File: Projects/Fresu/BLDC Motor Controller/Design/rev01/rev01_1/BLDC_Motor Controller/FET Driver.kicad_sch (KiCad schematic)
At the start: 0 parts

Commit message: UPDATE 7
COMPLETED MOSFET SCHEMATIC
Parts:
- added C18, C19, C20, C21, C25: 2u2, symbol Device:C
- added C22, C29: 10n, symbol Device:C
- added C23: 120p, symbol Device:C
- added C24: 22n, symbol Device:C
- added C26, C27, C28, C31, C34, C37: 100n, symbol Device:C
- added C30, C32, C33, C35, C36, C38, C39, C40, C41: 10u, symbol Device:C
- added D7: PMEG6020ELR, Diode_SMD:Nexperia_CFP3_SOD-123W, symbol Diode:PMEG6020ELR
- added D8: BAT60A, Diode_SMD:D_SOD-323, symbol Diode:BAT60A
- added L1: 22u, symbol Device:L
- added NT1: NetTie_2, symbol Device:NetTie_2
- added R11: 16k, symbol Device:R
- added R12: 10k, symbol Device:R
- added R13: 205K, symbol Device:R
- added R14: 1M, symbol Device:R
- added R15, R17, R19, R21: 18K, symbol Device:R
- added R16, R20, R22: 2K2, symbol Device:R
- added R18: 3K3, symbol Device:R
- added U2: DRV8302_DCA_56, DCA56_6P35X3P61, symbol DRV8302:DRV8302_DCA_56
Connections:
- new net: C22.1, C23.1
- new net: C22.2, R11.1
- new net: C25.2, U2.27 (AVDD)
- new net +3V3: U2.24 (REF), U2.9 (M_OC)
- new net +5V: D8.1 (K)
- new net +5V_DRV: C39.2, C40.2, C41.2, D8.2 (A), L1.2, R17.2
- new net +VDC: C26.2, C27.2, C28.2, C30.2, C32.2, C33.2, C35.2, C36.2, C38.2, U2.29 (PVDD1), U2.53 (PVDD2), U2.54 (PVDD2)
- new net BIAS: R14.1, U2.49 (BIAS)
- new net BR_S01: U2.25 (SO1)
- new net BR_S02: U2.26 (SO2)
- new net BST_A: C31.2, U2.48 (BST_A)
- new net BST_B: C34.2, U2.43 (BST_B)
- new net BST_BK: C29.1, U2.52 (BST_BK)
- new net BST_C: C37.2, U2.38 (BST_C)
- new net COMP: C23.2, R11.2, U2.2 (COMP)
- new net CP1: C24.2, U2.14 (CP1)
- new net CP2: C24.1, U2.15 (CP2)
- new net DC_CAL: U2.12 (DC_CAL)
- new net DTC: R12.2, U2.7 (DTC)
- new net DVDD: NT1.1, U2.23 (DVDD)
- new net EN_GATE: U2.16 (EN_GATE)
- new net FAULT: U2.6 (*FAULT)
- new net GND: C18.1, C19.1, C20.1, C21.1, C25.1, C26.1, C27.1, C28.1, C30.1, C32.1, C33.1, C35.1, C36.1, C38.1, C39.1, C40.1, C41.1, D7.2 (A), R12.1, R13.1, R14.2, R16.1, R18.1, R20.1, R22.1, U2.10 (GAIN), U2.28 (AGND), U2.57 (EPAD), U2.8 (M_PWM)
- new net GVDD: C18.2, C20.2, U2.13 (GVDD)
- new net H1: U2.17 (INH_A)
- new net H1_LOW: U2.44 (SL_A)
- new net H1_VS: C31.1, R21.2, U2.46 (SH_A)
- new net H2: U2.19 (INH_B)
- new net H2_LOW: U2.39 (SL_B)
- new net H2_VS: C34.1, R19.2, U2.41 (SH_B)
- new net H3: U2.21 (INH_C)
- new net H3_LOW: U2.34 (SL_C)
- new net H3_VS: C37.1, R15.2, U2.36 (SH_C)
- new net L1: U2.18 (INL_A)
- new net L2: U2.20 (INL_B)
- new net L3: U2.22 (INL_C)
- new net M_H1: U2.47 (GH_A)
- new net M_H2: U2.42 (GH_B)
- new net M_H3: U2.37 (GH_C)
- new net M_L1: U2.45 (GL_A)
- new net M_L2: U2.40 (GL_B)
- new net M_L3: U2.35 (GL_C)
- new net OC_ADJ: C19.2, C21.2, NT1.2, U2.11 (OC_ADJ)
- new net PH: C29.2, D7.1 (K), L1.1, U2.50 (PH), U2.51 (PH)
- new net RT_CLK: R13.2, U2.1 (RT_CLK)
- new net S1_N: U2.33 (SN1)
- new net S1_P: U2.32 (SP1)
- new net S2_N: U2.31 (SN2)
- new net S2_P: U2.30 (SP2)
- new net SENS1: R15.1, R16.2
- new net SENS2: R19.1, R20.2
- new net SENS3: R21.1, R22.2
- new net VSENSE: U2.3 (VSENSE)
- new net V_SENSE: R17.1, R18.2
- no-connect marks 0 -> 4
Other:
- note added: "ADD FAULT PULL UP"
- note added: "BOOTSTRAP CAPs"
- note added: "Hx_VS"
- note added: "INPUT PORTS"
- note added: "MCU SENSING FEEDBACK FOR EACH PHASE"
- note added: "OUTPUT PORTS"
- note added: "PHASE_1"
- note added: "PHASE_2"
- note added: "PHASE_3"
- note added: "SENSE 1 - PHASE 1"
- note added: "SENSE 2 - PHASE 2"

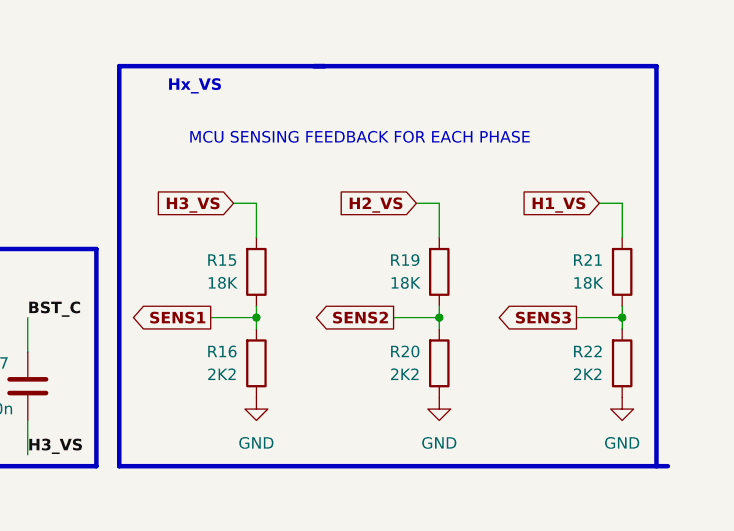
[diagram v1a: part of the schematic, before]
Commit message: Update 13
Added:
1) USB Schematic
2) footprints to all parts
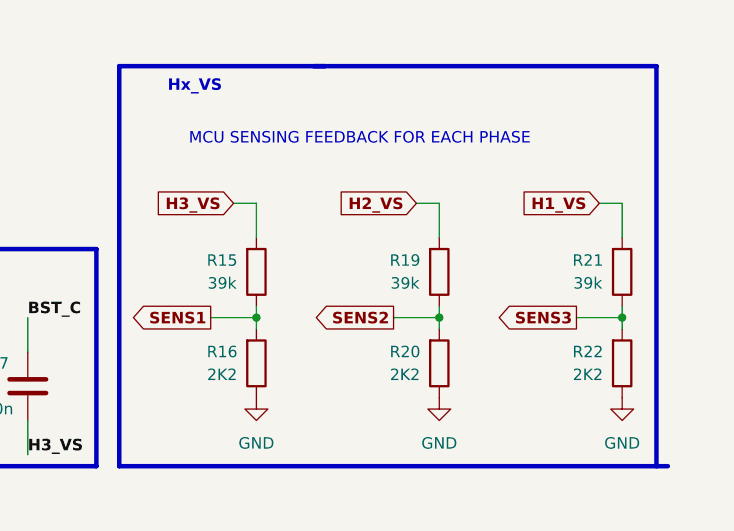
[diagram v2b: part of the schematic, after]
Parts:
- C18, C19, C20, C21, C22, C23, C24, C25, C26, C27, C28, C29, C30, C31, C32, C33, C34, C35, C36, C37, C38, C39, C40, C41: footprint (none) -> Capacitor_SMD:C_0603_1608Metric
- L1: footprint (none) -> DF_ESC_Footprint_Library:IND-SMD_L7.8-W7.8_SDR0805
- NT1: footprint (none) -> DF_ESC_Footprint_Library:NetTie_SMD_Pad_0.2mm
- R11, R12, R13, R14, R16, R17, R18, R20, R22: footprint (none) -> Resistor_SMD:R_0603_1608Metric_Pad0.98x0.95mm_HandSolder
- R15, R19, R21: value 18K -> 39k; footprint (none) -> Resistor_SMD:R_0603_1608Metric_Pad0.98x0.95mm_HandSolder
- U2: footprint DCA56_6P35X3P61 -> Package_SO:HTSSOP-56-1EP_6.1x14mm_P0.5mm_EP3.61x6.35mm

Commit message: Update 15
Fixing some schematic errors

initial layout of larger component complete
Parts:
- C29: value 10n -> 100n
- C30, C32, C33, C35, C36, C38: value 10u -> 1u
- renumbered R11 to R12, R12 to R13, R13 to R14, R14 to R15, R15 to R16, R16 to R17, R17 to R18, R18 to R19, R19 to R20, R20 to R21, R21 to R22, R22 to R23

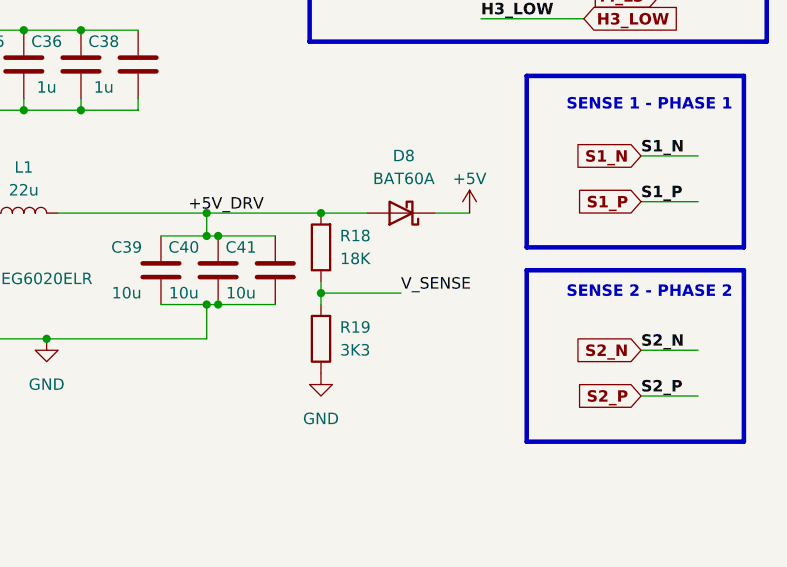
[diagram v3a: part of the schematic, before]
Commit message: Update 16
Almost finished placing all the components on the board as rough placement
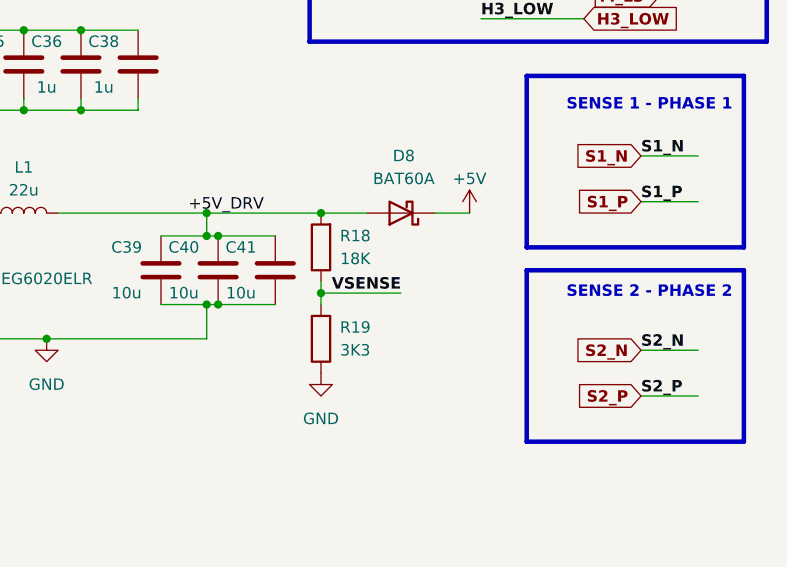
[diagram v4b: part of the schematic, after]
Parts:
- C39, C40, C41: footprint Capacitor_SMD:C_0603_1608Metric -> Capacitor_SMD:C_1206_3216Metric
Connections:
- net V_SENSE is gone; now on net VSENSE: R18.1, R19.2
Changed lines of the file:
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@@
+    (effects (font (size 1.27 1.27) bold) (justify right bottom))
+  )
+  (label "VSENSE" (at 238.76 85.09 180) (fields_autoplaced)
     (effects (font (size 1.27 1.27) bold) (justify right bottom))
   )
@@
   (label "H3_VS" (at 160.02 116.84 0) (fields_autoplaced)
     (effects (font (size 1.27 1.27) bold) (justify left bottom))
-  )
-  (label "V_SENSE" (at 238.76 85.09 0) (fields_autoplaced)
-    (effects (font (size 1.27 1.27)) (justify left bottom))
   )
   (label "H3" (at 31.75 57.15 180) (fields_autoplaced)
@@
       (effects (font (size 1.27 1.27)))
     )
-    (property "Footprint" "Capacitor_SMD:C_0603_1608Metric" (at 223.8248 78.74 0)
+    (property "Footprint" "Capacitor_SMD:C_1206_3216Metric" (at 223.8248 78.74 0)
       (effects (font (size 1.27 1.27)) hide)
     )
@@
       (effects (font (size 1.27 1.27)))
     )
-    (property "Footprint" "Capacitor_SMD:C_0603_1608Metric" (at 211.1248 78.74 0)
+    (property "Footprint" "Capacitor_SMD:C_1206_3216Metric" (at 211.1248 78.74 0)
       (effects (font (size 1.27 1.27)) hide)
     )
@@
       (effects (font (size 1.27 1.27)))
     )
-    (property "Footprint" "Capacitor_SMD:C_0603_1608Metric" (at 217.4748 78.74 0)
-      (effects (font (size 1.27 1.27)) hide)
-    )
+    (property "Footprint" "Capacitor_SMD:C_1206_3216Metric" (at 217.4748 78.74 0)
+      (effects (font (size 1.27 1.27)) hide)
+    )

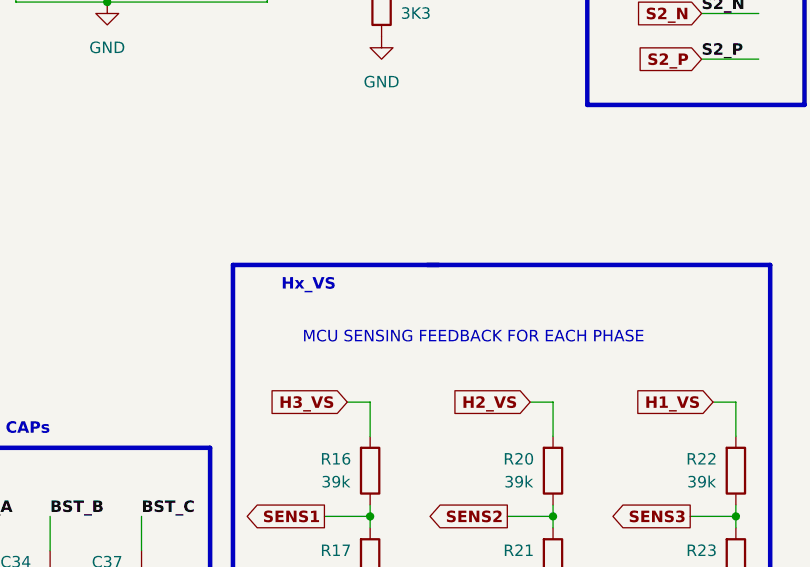
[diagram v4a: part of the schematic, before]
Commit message: Update 17
Started laying out the driver and the main FET power polygons
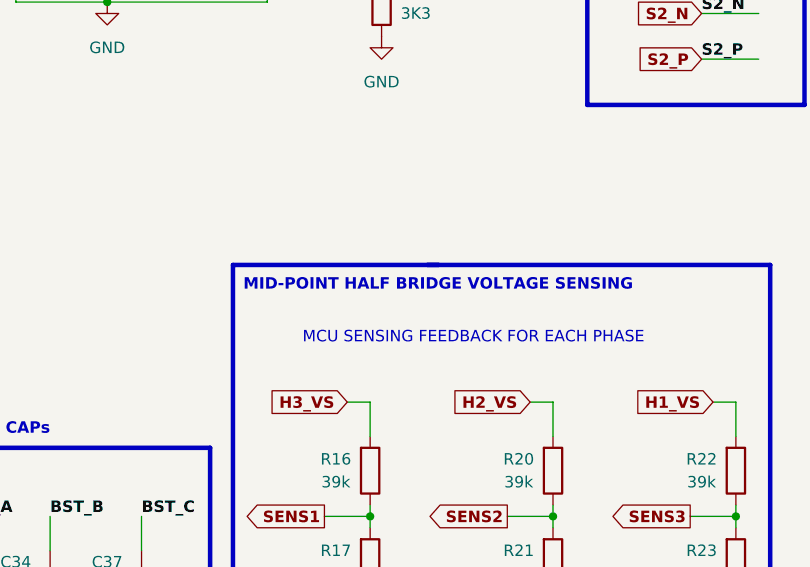
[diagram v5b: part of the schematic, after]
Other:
- note added: "MID-POINT HALF BRIDGE VOLTAGE SENSING"
- note removed: "Hx_VS"
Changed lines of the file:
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@@
     (effects (font (size 1.27 1.27) bold) (justify right bottom))
   )
-  (text "Hx_VS\n\n" (at 224.79 124.46 0)
+  (text "MID-POINT HALF BRIDGE VOLTAGE SENSING \n\n" (at 257.81 124.46 0)
     (effects (font (size 1.27 1.27) bold) (justify right bottom))
   )

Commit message: Update 26
Matched DF's Designators to mine so I can use BOM as is

Updated MFR'ing files

Rev1 Ready for release
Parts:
- renumbered C19 to C23, C18 to C24, C22 to C25, C21 to C26, C20 to C27, C23 to C28, C24 to C29, C25 to C30, C26 to C31, C27 to C32, C29 to C33, C28 to C34, C31 to C35, C30 to C36, C32 to C37, C33 to C38, C34 to C39, C35 to C40, C36 to C41, C39 to C42, C37 to C43, C38 to C44, C40 to C59, C41 to C60, D7 to D12, D8 to D13, R18 to R16, R19 to R17, R16 to R18, R17 to R19, U2 to U3
